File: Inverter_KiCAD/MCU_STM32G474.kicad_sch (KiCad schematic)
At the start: 18 parts, among them J2 Conn_ST_STDC14, SW1 SW_Push, SW2 SW_Push, U18 STM32G474RETx, Y1 16M

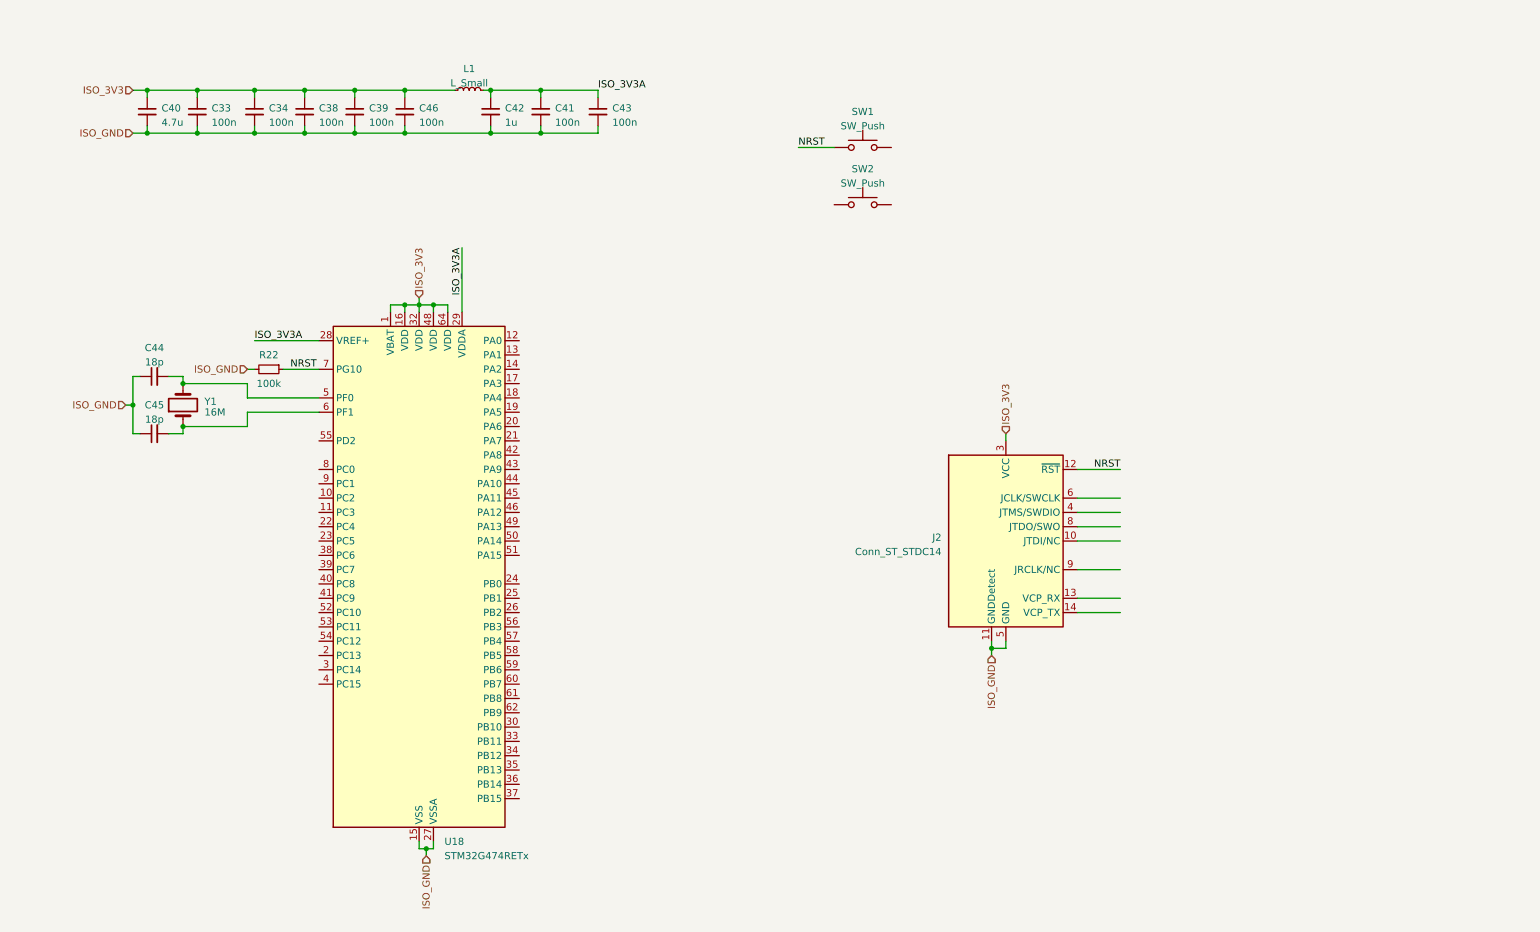
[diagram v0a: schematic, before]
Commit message: update schematic
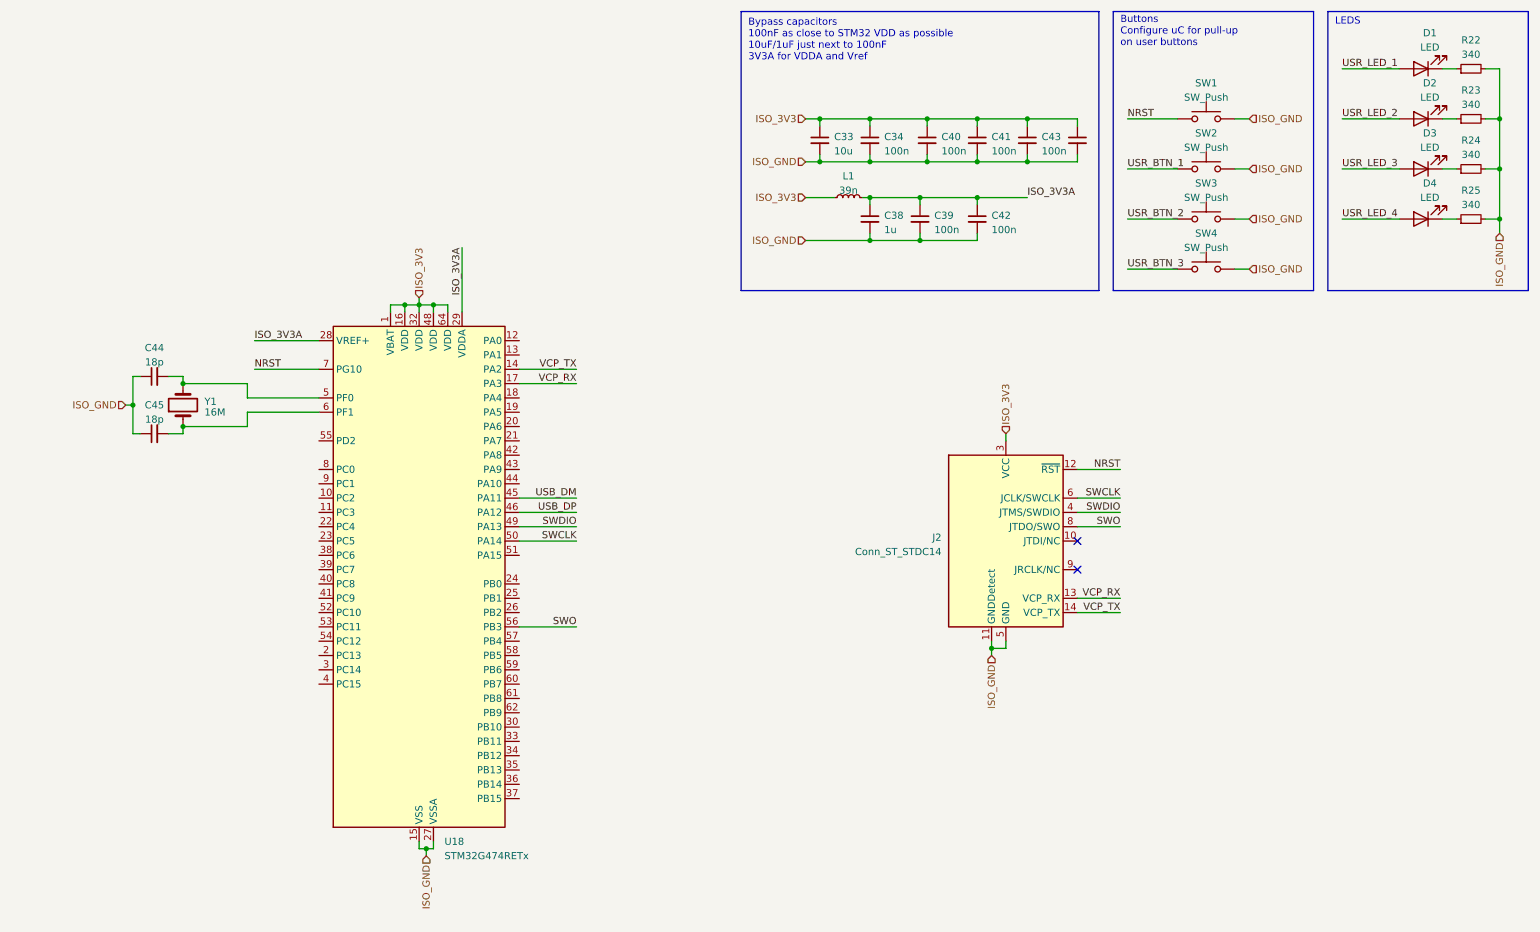
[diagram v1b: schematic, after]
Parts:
- added D1, D2, D3, D4: LED, symbol Device:LED
- added R23, R24, R25: 340, symbol Device:R_Small
- added SW3, SW4: SW_Push, symbol Switch:SW_Push
- C33: value 100n -> 10u
- C38: value 100n -> 1u
- C40: value 4.7u -> 100n
- C42: value 1u -> 100n
- J2: footprint (none) -> Connector_PinHeader_1.27mm:PinHeader_2x07_P1.27mm_Vertical_SMD
- L1: value L_Small -> 39n
- R22: value 100k -> 340
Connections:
- net ISO_3V3: now also C41.1, C43.1; no longer C38.1, C39.1
- net ISO_3V3A: now also C38.1, C39.1; no longer C41.1, C43.1
- net ISO_GND: now also SW1.2, SW2.2, R23.2, R24.2, R25.2, SW3.2, SW4.2
- net NRST: no longer R22.1
- net VCP_RX: now reaches J2.13 (VCP_RX)
- net VCP_RX: now also U18.17 (PA3)
- net VCP_TX: now reaches J2.14 (VCP_TX)
- net VCP_TX: now also U18.14 (PA2)
- net SWDIO: now reaches J2.4 (JTMS/SWDIO)
- net SWDIO: now also U18.49 (PA13)
- net SWCLK: now reaches J2.6 (JCLK/SWCLK)
- net SWCLK: now also U18.50 (PA14)
- net SWO: now reaches J2.8 (JTDO/SWO)
- net SWO: now also U18.56 (PB3)
- net USB_DM: now reaches U18.45 (PA11)
- net USB_DP: now reaches U18.46 (PA12)
- net USR_BTN_1: now reaches SW2.1
- new net: D2.1 (K), R23.1
- new net: D1.1 (K), R22.1
- new net: D3.1 (K), R24.1
- new net: D4.1 (K), R25.1
- new net USR_BTN_2: SW3.1
- new net USR_BTN_3: SW4.1
- new net USR_LED_1: D1.2 (A)
- new net USR_LED_2: D2.2 (A)
- new net USR_LED_3: D3.2 (A)
- new net USR_LED_4: D4.2 (A)
- no-connect marks 0 -> 2
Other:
- note added: "Buttons Configure uC for pull-up on user buttons"
- note added: "Bypass capacitors 100nF as close to STM32 VDD as possible 10uF/1uF just next to 100nF 3V3A for VDDA and Vref"
- note added: "LEDS"
- moved on the sheet: SW1, SW2

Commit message: add break
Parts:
- added C50, C51: 10u, Capacitor_SMD:C_0603_1608Metric_Pad1.08x0.95mm_HandSolder, symbol Device:C_Small
- added C52, C53, C54, C55, C56: 100n, Capacitor_SMD:C_0402_1005Metric_Pad0.74x0.62mm_HandSolder, symbol Device:C_Small
- added J3: Conn_01x04, Connector_JST:JST_XH_B4B-XH-A_1x04_P2.50mm_Vertical, symbol Connector_Generic:Conn_01x04
- added J4: Conn_01x05, Connector_JST:JST_XH_B5B-XH-A_1x05_P2.50mm_Vertical, symbol Connector_Generic:Conn_01x05
- added J5: USB_C_Receptacle_USB2.0, Connector_USB:USB_C_Receptacle_HRO_TYPE-C-31-M-12, symbol Connector:USB_C_Receptacle_USB2.0
- added R26: 10k, Resistor_SMD:R_0603_1608Metric_Pad0.98x0.95mm_HandSolder, symbol Device:R_Small
- added R27, R28: 5.1k, Resistor_SMD:R_0603_1608Metric_Pad0.98x0.95mm_HandSolder, symbol Device:R_Small
- added SW5: SW_Push, Button_Switch_SMD:SW_SPST_B3U-3000P, symbol Switch:SW_Push
- added U20: USBLC6-2SC6, Package_TO_SOT_SMD:SOT-23-6, symbol Power_Protection:USBLC6-2SC6
- C33, C38: footprint (none) -> Capacitor_SMD:C_0603_1608Metric_Pad1.08x0.95mm_HandSolder
- C34, C39, C40, C41, C42, C43, C44, C45, C46: footprint (none) -> Capacitor_SMD:C_0402_1005Metric_Pad0.74x0.62mm_HandSolder
- D1, D2, D3, D4: footprint (none) -> LED_SMD:LED_0603_1608Metric_Pad1.05x0.95mm_HandSolder
- L1: footprint (none) -> Inductor_SMD:L_0603_1608Metric_Pad1.05x0.95mm_HandSolder
- R22, R23, R24, R25: footprint (none) -> Resistor_SMD:R_0603_1608Metric_Pad0.98x0.95mm_HandSolder
- SW1, SW2, SW3, SW4: footprint (none) -> Button_Switch_SMD:SW_SPST_B3U-3000P
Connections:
- net ISO_3V3: now also C50.2, C51.1, J3.1 (Pin_1), J4.1 (Pin_1)
- net ISO_GND: now also C50.1, C51.2, C52.2, C53.2, C54.2, C55.2, C56.2, J3.2 (Pin_2), J4.2 (Pin_2), J5.A1 (GND), J5.A12 (GND), J5.B1 (GND), J5.B12 (GND), R26.2, R27.2, R28.2, SW5.2, U20.2 (GND)
- net NRST: now also C56.1
- net USB_DM: now also U20.3 (I/O2)
- net USB_DP: now also U20.1 (I/O1)
- net USR_BTN_1: now also U18.55 (PD2), C55.1
- net USR_BTN_2: now also U18.57 (PB4), C54.1
- net USR_BTN_3: now also U18.59 (PB6), C53.1
- net USR_LED_1: now also U18.51 (PA15)
- net USR_LED_2: now also U18.52 (PC10)
- net USR_LED_3: now also U18.53 (PC11)
- net USR_LED_4: now also U18.54 (PC12)
- net VCP_RX: now also U18.33 (PB11); no longer U18.17 (PA3)
- net VCP_TX: now also U18.30 (PB10); no longer U18.14 (PA2)
- net U_VPh: now reaches U18.12 (PA0)
- net U_Imes: now reaches U18.13 (PA1)
- net ENC_BTN: now reaches U18.19 (PA5)
- net ENC_BTN: now also J4.5 (Pin_5)
- net ENC_A: now reaches U18.20 (PA6)
- net ENC_A: now also J4.3 (Pin_3)
- net ENC_B: now reaches U18.21 (PA7)
- net ENC_B: now also J4.4 (Pin_4)
- net Nucleo_Tx: now reaches U18.22 (PC4)
- net Nucleo_Rx: now reaches U18.23 (PC5)
- net Nucleo_NRST: now reaches U18.24 (PB0)
- net W_VPh: now reaches U18.25 (PB1)
- net Bus_V: now reaches U18.34 (PB12)
- net W_Imes: now reaches U18.35 (PB13)
- net Bus_Imes: now reaches U18.36 (PB14)
- net Pwr_Enable: now reaches U18.37 (PB15)
- net IC_PWN_V_H: now reaches U18.38 (PC6)
- net IC_PWN_V_L: now reaches U18.39 (PC7)
- net IC_PWN_W_H: now reaches U18.40 (PC8)
- net IC_PWN_W_L: now reaches U18.41 (PC9)
- net Screen_SDA: now reaches U18.42 (PA8)
- net Screen_SDA: now also J3.4 (Pin_4)
- net Screen_SCL: now reaches U18.43 (PA9)
- net Screen_SCL: now also J3.3 (Pin_3)
- net ISO_PWM_Break: now reaches U18.58 (PB5)
- net Soft_NRST: now reaches U18.60 (PB7)
- net Soft_NRST: now also C52.1, SW5.1
- net at U18.61 (PB8): now also R26.1
- net V_VPh: now reaches U18.8 (PC0)
- net V_Imes: now reaches U18.9 (PC1)
- new net: J5.B5 (CC2), R28.1
- new net: J5.A5 (CC1), R27.1
- new net D+: J5.A6 (D+), J5.B6 (D+), U20.6 (I/O1)
- new net D-: J5.A7 (D-), J5.B7 (D-), U20.4 (I/O2)
- new net IC_PWN_U_H: U18.14 (PA2)
- new net IC_PWN_U_L: U18.17 (PA3)
- new net V_USB: J5.A4 (VBUS), J5.A9 (VBUS), J5.B4 (VBUS), J5.B9 (VBUS), U20.5 (VBUS)
- no-connect marks 2 -> 14
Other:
- note added: "Connector for Encodeur"
- note added: "I2C connector for display MDOB128064XV-YI"
- note added: "PBOOT0 - PB8"
- note added: "PC4 - USART1_TX PC5 - USART1_RX"
- note added: "ST-Link"
- note added: "STM32G474RET6 uC"
- note added: "USB connector + ESD protection 90 ohm impedance"
- moved on the sheet: C44, C45, J2, SW1, SW2, SW3, SW4, U18, Y1

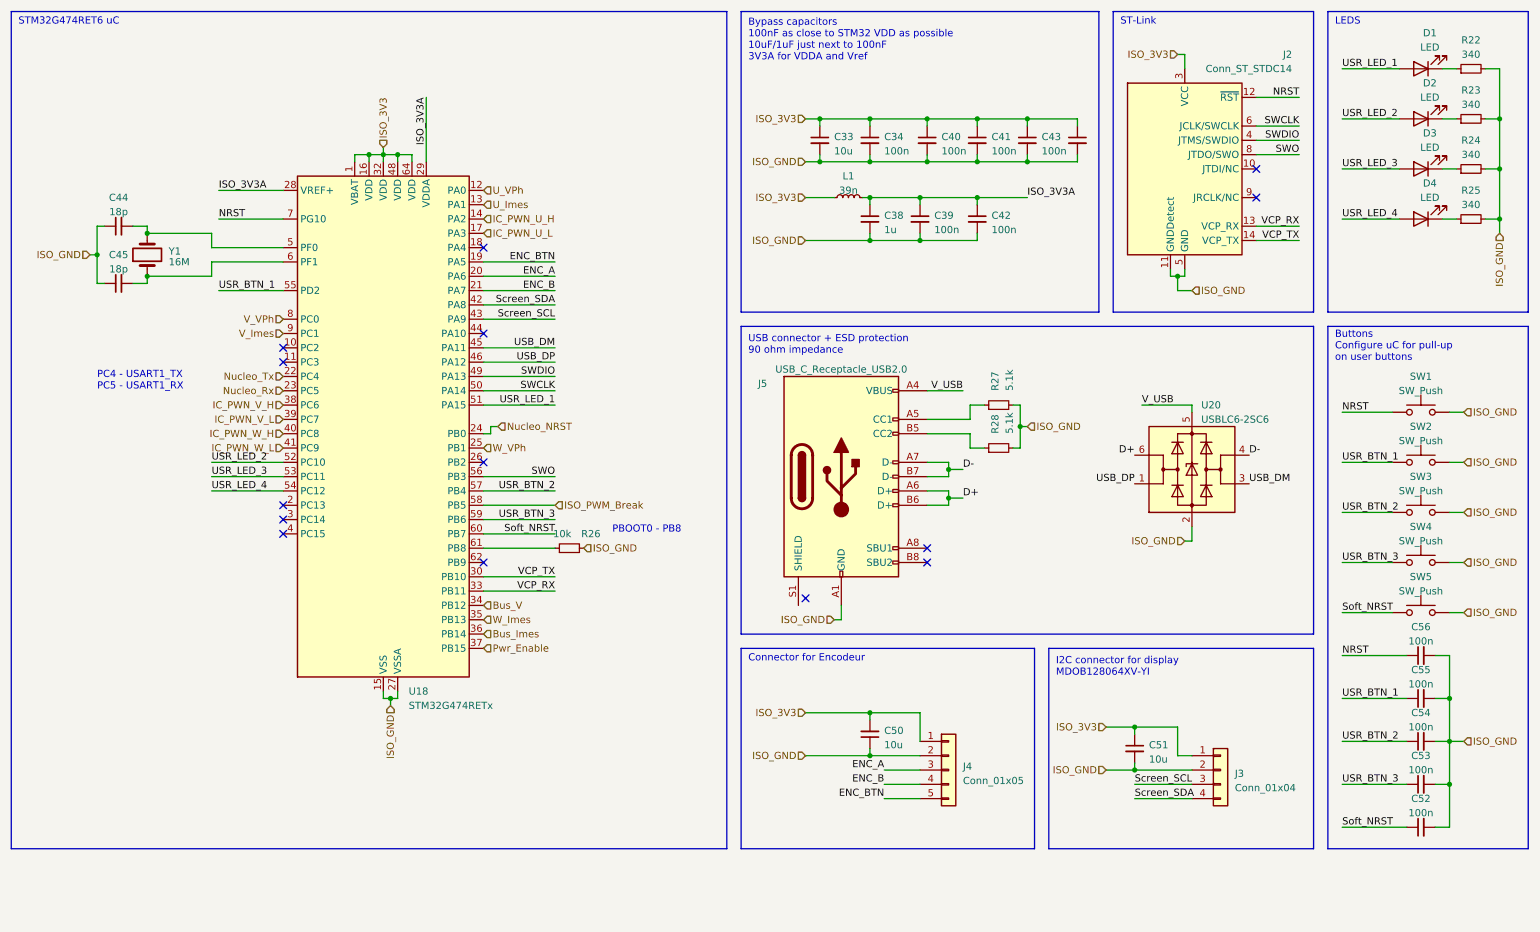
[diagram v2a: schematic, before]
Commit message: clear schematic errors
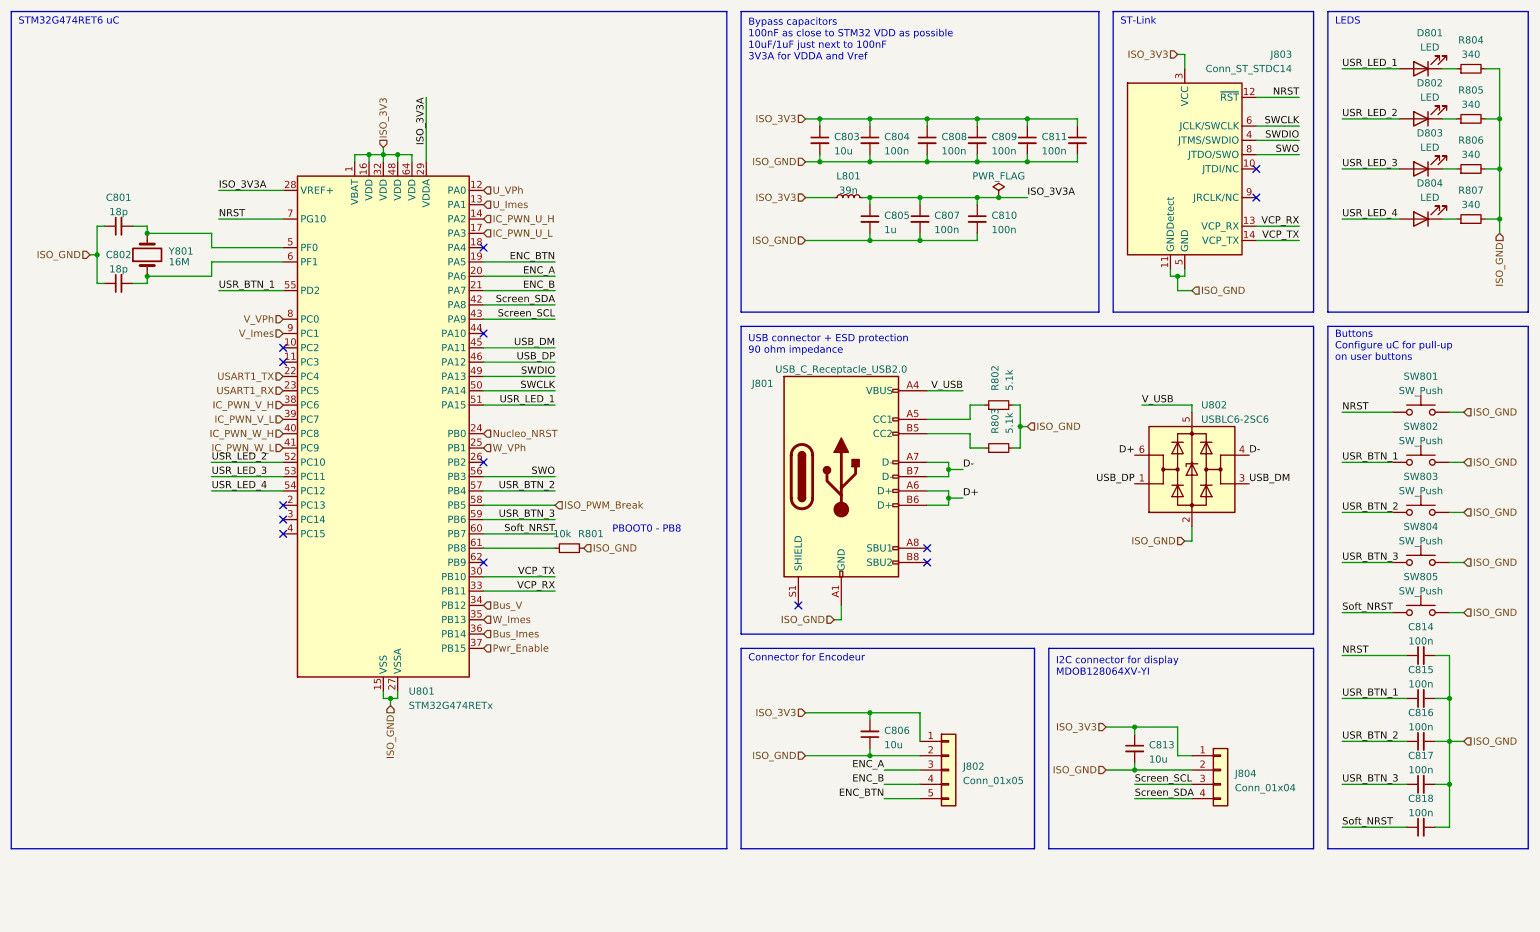
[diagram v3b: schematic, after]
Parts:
- renumbered C44 to C801, C45 to C802, C33 to C803, C34 to C804, C38 to C805, C50 to C806, C39 to C807, C40 to C808, C41 to C809, C42 to C810, C43 to C811, C46 to C812, C51 to C813, C56 to C814, C55 to C815, C54 to C816, C53 to C817, C52 to C818, D1 to D801, D2 to D802, D3 to D803, D4 to D804, J5 to J801, J4 to J802, J2 to J803, J3 to J804, L1 to L801, R26 to R801, R27 to R802, R28 to R803, R22 to R804, R23 to R805, R24 to R806, R25 to R807, SW1 to SW801, SW2 to SW802, SW3 to SW803, SW4 to SW804, SW5 to SW805, U18 to U801, U20 to U802, Y1 to Y801
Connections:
- net Nucleo_Rx renamed USART1_RX
- net Nucleo_Tx renamed USART1_TX
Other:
- note removed: "PC4 - USART1_TX PC5 - USART1_RX"
